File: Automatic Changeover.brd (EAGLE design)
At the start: 160 x 148.3 mm, 49 parts, among them IC1 ACS750LCA-050, IC2 XMEGA16A4A, IC4 ACS750LCA-050, IC5 ACS750LCA-050, K1 S216SE1, K2 S216SE1, K3 S216SE1, K4 S216SE1, K5 S216SE1, K6 S216SE1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

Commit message: placed all components on board
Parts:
- moved -SOURCE0 262.3 mm to (151.1, 142.2), turned to 270 degrees
- moved +SOURCE0 258.5 mm to (144.8, 142.2), turned to 270 degrees
- moved -SOURCE1 255.0 mm to (138.4, 142.2), turned to 270 degrees
- moved +SOURCE1 251.7 mm to (132.1, 142.2), turned to 270 degrees
- moved +SOURCE2 248.8 mm to (125.7, 142.2), turned to 270 degrees
- moved -SOURCE2 246.1 mm to (119.4, 142.2), turned to 270 degrees
- moved K1 212.1 mm to (137.2, 111.8)
- moved K2 212.1 mm to (119.4, 111.8)
- moved K3 212.1 mm to (101.6, 111.8)
- moved K4 159.9 mm to (137.2, 125.7)
- moved K5 159.9 mm to (119.4, 125.7)
- moved K6 159.9 mm to (101.6, 125.7)
- moved DC1 155.4 mm to (38.1, 69.8)
- moved -OUTLET0 148.7 mm to (80.0, 142.2)
- moved OK1 148.7 mm to (68.6, 127.0)
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
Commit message: rearranged the crystal and capactitor for it
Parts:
- moved C2 53.4 mm to (58.4, 99.1), turned to 90 degrees
- moved C1 53.4 mm to (64.8, 99.1), turned to 90 degrees
- moved C4 23.4 mm to (38.1, 90.2)
- moved X4 2.54 mm to (62.2, 91.4)
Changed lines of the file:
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@@
 <attribute name="VALUE" x="140.97" y="15.24" size="1.778" layer="27" ratio="10"/>
 </element>
-<element name="C1" library="rcl" library_urn="urn:adsk.eagle:library:334" package="C025-025X050" package3d_urn="urn:adsk.eagle:package:23629/2" value="" x="16.51" y="121.92" smashed="yes">
-<attribute name="NAME" x="14.224" y="123.444" size="1.27" layer="25" ratio="10"/>
-<attribute name="POPULARITY" value="65" x="133.35" y="-26.67" size="1.778" layer="27" display="off"/>
-<attribute name="SPICEPREFIX" value="C" x="133.35" y="-26.67" size="1.778" layer="27" display="off"/>
-<attribute name="VALUE" x="14.224" y="119.126" size="1.27" layer="27" ratio="10"/>
-</element>
-<element name="C2" library="rcl" library_urn="urn:adsk.eagle:library:334" package="C025-025X050" package3d_urn="urn:adsk.eagle:package:23629/2" value="" x="10.16" y="121.92" smashed="yes">
-<attribute name="NAME" x="7.874" y="123.444" size="1.27" layer="25" ratio="10"/>
-<attribute name="POPULARITY" value="65" x="133.35" y="-26.67" size="1.778" layer="27" display="off"/>
-<attribute name="SPICEPREFIX" value="C" x="133.35" y="-26.67" size="1.778" layer="27" display="off"/>
-<attribute name="VALUE" x="7.874" y="119.126" size="1.27" layer="27" ratio="10"/>
+<element name="C1" library="rcl" library_urn="urn:adsk.eagle:library:334" package="C025-025X050" package3d_urn="urn:adsk.eagle:package:23629/2" value="" x="64.77" y="99.06" smashed="yes" rot="R90">
+<attribute name="NAME" x="63.246" y="96.774" size="1.27" layer="25" ratio="10" rot="R90"/>
+<attribute name="POPULARITY" value="65" x="213.36" y="215.9" size="1.778" layer="27" rot="R90" display="off"/>
+<attribute name="SPICEPREFIX" value="C" x="213.36" y="215.9" size="1.778" layer="27" rot="R90" display="off"/>
+<attribute name="VALUE" x="67.564" y="96.774" size="1.27" layer="27" ratio="10" rot="R90"/>
+</element>
+<element name="C2" library="rcl" library_urn="urn:adsk.eagle:library:334" package="C025-025X050" package3d_urn="urn:adsk.eagle:package:23629/2" value="" x="58.42" y="99.06" smashed="yes" rot="R90">
+<attribute name="NAME" x="56.896" y="96.774" size="1.27" layer="25" ratio="10" rot="R90"/>
+<attribute name="POPULARITY" value="65" x="207.01" y="222.25" size="1.778" layer="27" rot="R90" display="off"/>
+<attribute name="SPICEPREFIX" value="C" x="207.01" y="222.25" size="1.778" layer="27" rot="R90" display="off"/>
+<attribute name="VALUE" x="61.214" y="96.774" size="1.27" layer="27" ratio="10" rot="R90"/>
 </element>
 <element name="C3" library="capacitor-wima" library_urn="urn:adsk.eagle:library:116" package="C2.5-2" package3d_urn="urn:adsk.eagle:package:5415/1" value="10V 100u" x="13.97" y="115.57" smashed="yes">
@@
 <attribute name="VALUE" x="12.319" y="112.776" size="1.27" layer="27" ratio="10"/>
 </element>
-<element name="C4" library="capacitor-wima" library_urn="urn:adsk.eagle:library:116" package="C2.5-2" package3d_urn="urn:adsk.eagle:package:5415/1" value="400V 10u" x="55.88" y="105.41" smashed="yes">
-<attribute name="NAME" x="54.229" y="106.934" size="1.27" layer="25" ratio="10"/>
-<attribute name="POPULARITY" value="28" x="76.2" y="-44.45" size="1.778" layer="27" display="off"/>
-<attribute name="VALUE" x="54.229" y="102.616" size="1.27" layer="27" ratio="10"/>
+<element name="C4" library="capacitor-wima" library_urn="urn:adsk.eagle:library:116" package="C2.5-2" package3d_urn="urn:adsk.eagle:package:5415/1" value="400V 10u" x="38.1" y="90.17" smashed="yes">
+<attribute name="NAME" x="36.449" y="91.694" size="1.27" layer="25" ratio="10"/>
+<attribute name="POPULARITY" value="28" x="58.42" y="-59.69" size="1.778" layer="27" display="off"/>
+<attribute name="VALUE" x="36.449" y="87.376" size="1.27" layer="27" ratio="10"/>
 </element>
 <element name="C5" library="capacitor-wima" library_urn="urn:adsk.eagle:library:116" package="C2.5-2" package3d_urn="urn:adsk.eagle:package:5415/1" value="25V 100n" x="45.72" y="105.41" smashed="yes">
@@
 <attribute name="VALUE" x="3.81" y="37.465" size="1.27" layer="27"/>
 </element>
-<element name="X4" library="IQD-Frequency-Products" library_urn="urn:adsk.eagle:library:90" package="HC49" package3d_urn="urn:adsk.eagle:package:3356/1" value="16MHz" x="62.23" y="93.98" smashed="yes">
-<attribute name="NAME" x="57.15" y="96.647" size="1.27" layer="25" ratio="10"/>
-<attribute name="POPULARITY" value="0" x="110.49" y="-39.37" size="1.778" layer="27" display="off"/>
-<attribute name="VALUE" x="57.15" y="90.043" size="1.27" layer="27" ratio="10"/>
+<element name="X4" library="IQD-Frequency-Products" library_urn="urn:adsk.eagle:library:90" package="HC49" package3d_urn="urn:adsk.eagle:package:3356/1" value="16MHz" x="62.23" y="91.44" smashed="yes">
+<attribute name="NAME" x="57.15" y="94.107" size="1.27" layer="25" ratio="10"/>
+<attribute name="POPULARITY" value="0" x="110.49" y="-41.91" size="1.778" layer="27" display="off"/>
+<attribute name="VALUE" x="57.15" y="87.503" size="1.27" layer="27" ratio="10"/>
 </element>
 <element name="-SOURCE0" library="wirepad" library_urn="urn:adsk.eagle:library:412" package="3,81/1,4" package3d_urn="urn:adsk.eagle:package:30835/1" value="" x="151.13" y="142.24" smashed="yes" rot="R270">
@@
 <wire x1="127" y1="111.76" x2="144.78" y2="111.76" width="0" layer="19" extent="1-1"/>
 <wire x1="109.22" y1="111.76" x2="127" y2="111.76" width="0" layer="19" extent="1-1"/>
-<wire x1="17.78" y1="121.92" x2="109.22" y2="111.76" width="0" layer="19" extent="1-1"/>
-<wire x1="11.43" y1="121.92" x2="17.78" y2="121.92" width="0" layer="19" extent="1-1"/>
+<wire x1="64.77" y1="100.33" x2="109.22" y2="111.76" width="0" layer="19" extent="1-1"/>
+<wire x1="58.42" y1="100.33" x2="64.77" y2="100.33" width="0" layer="19" extent="1-1"/>
 <wire x1="63.03" y1="82" x2="13.4112" y2="101.8794" width="0" layer="19" extent="1-1"/>
 <wire x1="68.03" y1="77.8" x2="63.03" y2="82" width="0" layer="19" extent="1-1"/>
@@
 <contactref element="C1" pad="1"/>
 <contactref element="IC2" pad="36"/>
-<wire x1="64.63" y1="82" x2="64.643" y2="93.98" width="0" layer="19" extent="1-1"/>
-<wire x1="15.24" y1="121.92" x2="64.643" y2="93.98" width="0" layer="19" extent="1-1"/>
+<wire x1="64.63" y1="82" x2="64.643" y2="91.44" width="0" layer="19" extent="1-1"/>
+<wire x1="64.77" y1="97.79" x2="64.643" y2="91.44" width="0" layer="19" extent="1-1"/>
 </signal>
 <signal name="XT1">
@@
 <contactref element="C2" pad="1"/>
 <contactref element="IC2" pad="37"/>
-<wire x1="63.83" y1="82" x2="59.817" y2="93.98" width="0" layer="19" extent="1-1"/>
-<wire x1="8.89" y1="121.92" x2="59.817" y2="93.98" width="0" layer="19" extent="1-1"/>
+<wire x1="63.83" y1="82" x2="59.817" y2="91.44" width="0" layer="19" extent="1-1"/>
+<wire x1="58.42" y1="97.79" x2="59.817" y2="91.44" width="0" layer="19" extent="1-1"/>
 </signal>
 <signal name="PDI_SCK">
@@
 <contactref element="B4" pad="-"/>
 <contactref element="B3" pad="-"/>
-<wire x1="46.99" y1="105.41" x2="57.15" y2="105.41" width="0" layer="19" extent="1-1"/>
+<wire x1="46.99" y1="105.41" x2="39.37" y2="90.17" width="0" layer="19" extent="1-1"/>
 <wire x1="46.99" y1="140.97" x2="46.99" y2="105.41" width="0" layer="19" extent="1-1"/>
 <wire x1="44.45" y1="140.97" x2="46.99" y2="140.97" width="0" layer="19" extent="1-1"/>
@@
 <contactref element="C4" pad="1"/>
 <contactref element="D3" pad="A"/>
-<wire x1="29.21" y1="133.35" x2="54.61" y2="105.41" width="0" layer="19" extent="1-1"/>
+<wire x1="29.21" y1="133.35" x2="36.83" y2="90.17" width="0" layer="19" extent="1-1"/>
 <wire x1="132.08" y1="57.15" x2="29.21" y2="133.35" width="0" layer="19" extent="1-1"/>
 <wire x1="48.26" y1="115.57" x2="132.08" y2="57.15" width="0" layer="19" extent="1-1"/>

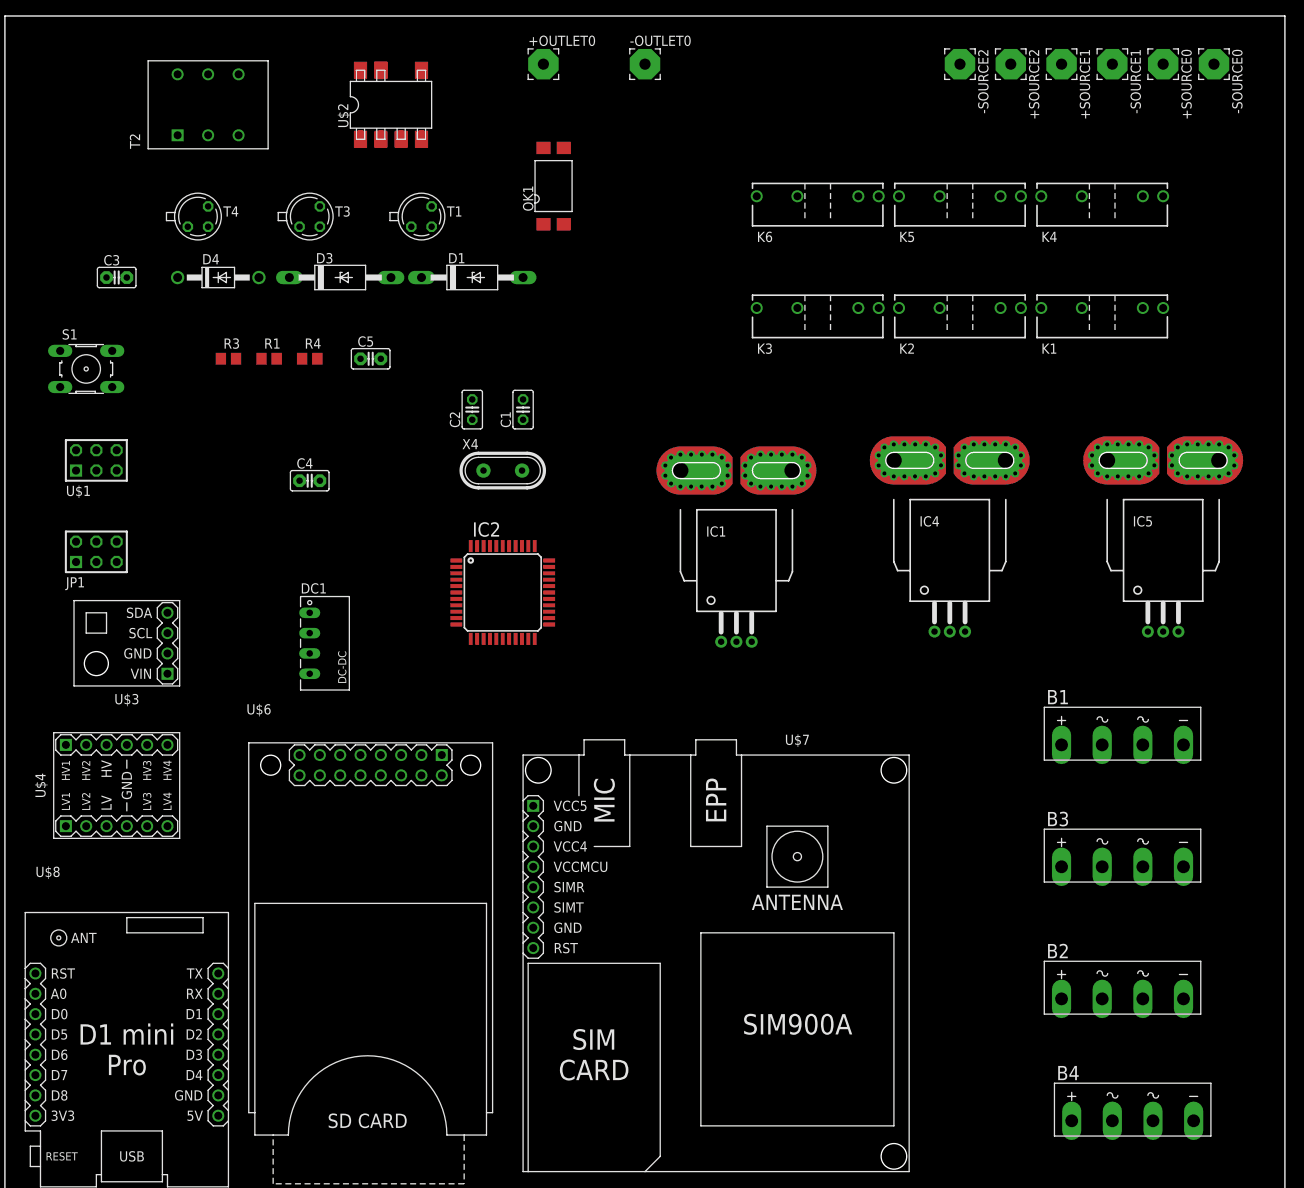
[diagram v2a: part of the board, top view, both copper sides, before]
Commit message: adjusted many components to desired position
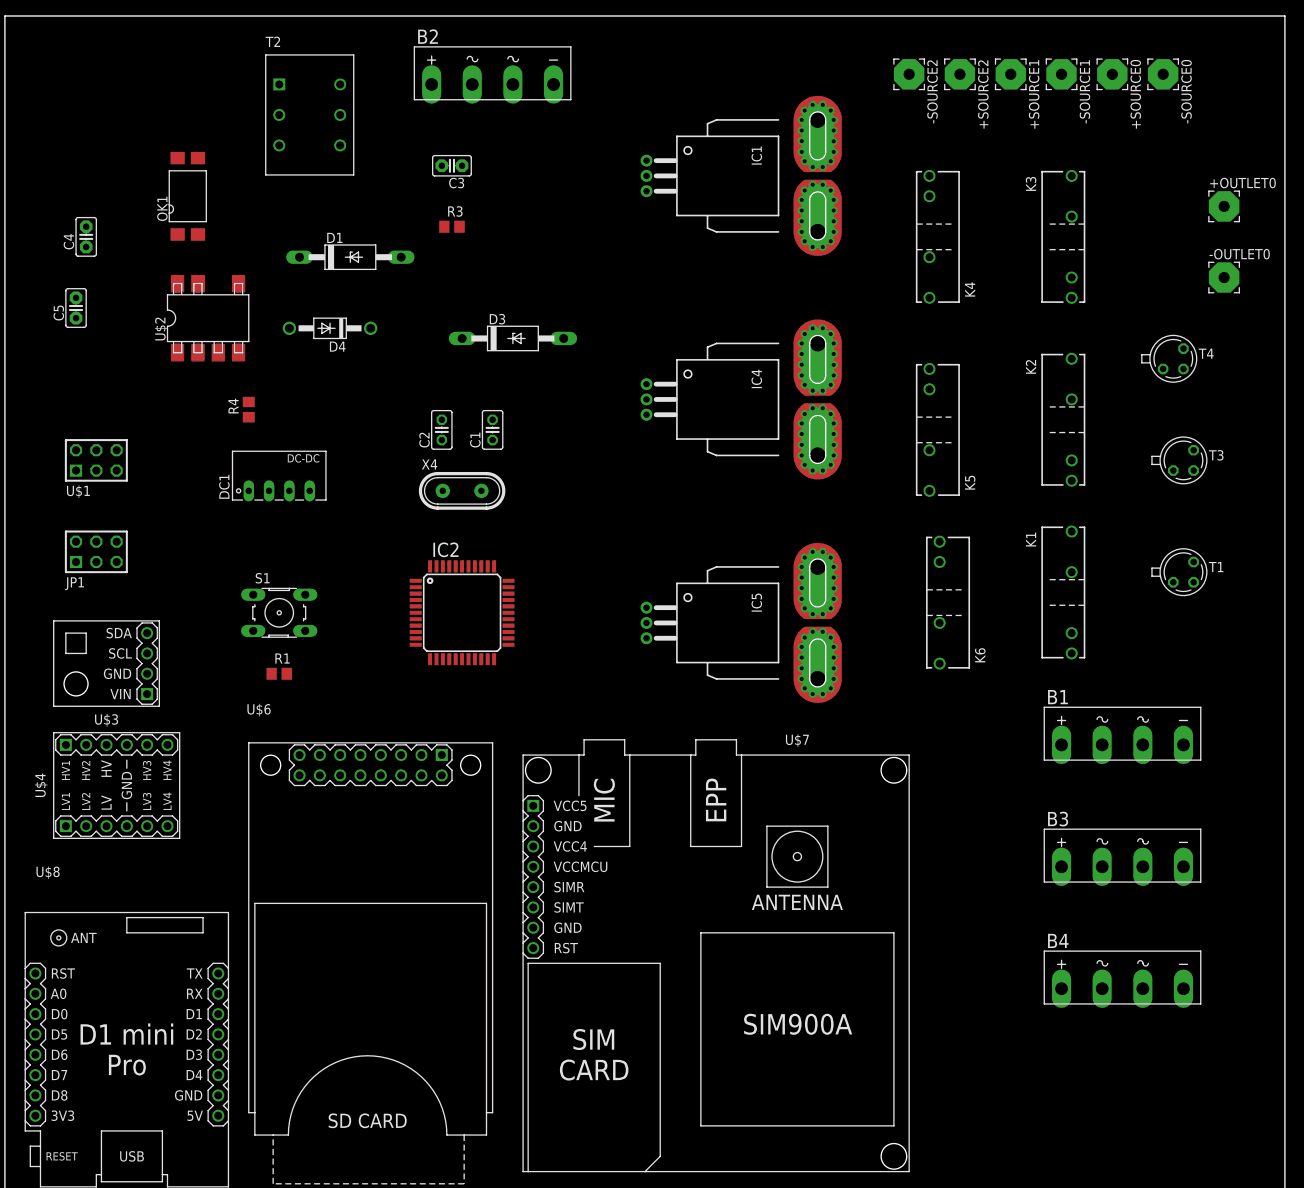
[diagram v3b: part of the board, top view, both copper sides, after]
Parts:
- moved B2 138.8 mm to (61.0, 141.0)
- moved T4 123.2 mm to (146.1, 105.4)
- moved T3 113.4 mm to (147.3, 92.7)
- moved T1 105.1 mm to (147.3, 78.7)
- moved +OUTLET0 86.9 mm to (152.4, 124.5)
- moved -OUTLET0 77.1 mm to (152.4, 115.6)
- moved K6 53.0 mm to (116.8, 74.9), turned to 90 degrees
- moved IC5 47.7 mm to (101.6, 72.4), turned to 270 degrees
- moved OK1 45.7 mm to (22.9, 125.7)
- moved C3 44.2 mm to (55.9, 129.5), turned to 180 degrees
- moved C4 41.3 mm to (10.2, 120.7), turned to 90 degrees
- moved R1 39.4 mm to (34.3, 66.0)
- moved S1 38.9 mm to (34.3, 73.7)
- moved IC1 38.2 mm to (101.6, 128.3), turned to 270 degrees
- moved C5 37.4 mm to (8.89, 111.8), turned to 90 degrees
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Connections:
- removed net N$15: C3.2
- net GND: now also C3.2
